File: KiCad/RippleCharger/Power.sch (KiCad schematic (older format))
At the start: 8 parts, among them J1 Screw_Terminal_01x02, U1 L7805

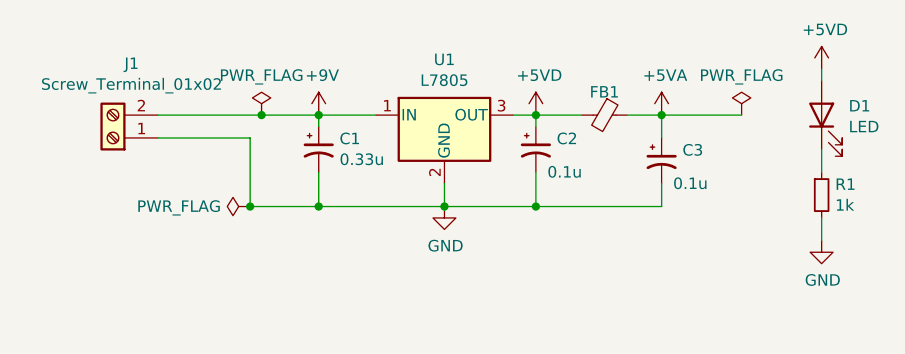
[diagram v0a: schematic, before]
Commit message: Update PCB layout m include relay footprint, board outlook.Modify Main 0049 code and add CV function
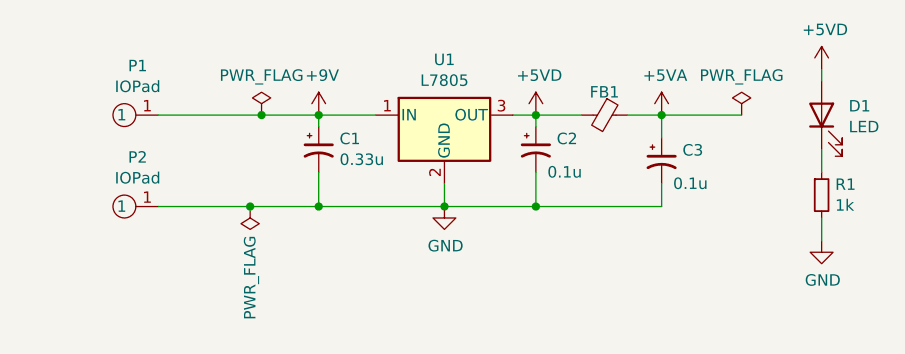
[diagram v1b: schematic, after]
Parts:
- removed J1: Screw_Terminal_01x02, TerminalBlock:TerminalBlock_Altech_AK300-2_P5.00mm, symbol Connector:Screw_Terminal_01x02
- added P1, P2: IOPad, basic:IOPad, symbol basic:IOPad
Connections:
- net +9V: now also P1.1
- net GND: now also P2.1
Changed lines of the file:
@@
 	1    0    0    -1
-$EndComp
-$Comp
-L Connector:Screw_Terminal_01x02 J1
-U 1 1 613EDB5C
-P 3200 3650
-F 0 "J1" H 3118 3325 50  0000 C CNN
-F 1 "Screw_Terminal_01x02" H 3118 3416 50  0000 C CNN
-F 2 "TerminalBlock:TerminalBlock_Altech_AK300-2_P5.00mm" H 3200 3650 50  0001 C CNN
-F 3 "~" H 3200 3650 50  0001 C CNN
-	1    3200 3650
-	-1   0    0    1
 $EndComp
 Wire Wire Line
 	3400 3550 3850 3550
-Wire Wire Line
-	3400 3650 3800 3650
-Wire Wire Line
-	3800 3650 3800 3950
 $Comp
 L power:PWR_FLAG #FLG02
@@
 F 3 "~" H 3800 3950 50  0001 C CNN
 	1    3800 3950
-	0    -1   -1   0
+	-1   0    0    1
 $EndComp
-Connection ~ 3800 3950
 $Comp
 L power:PWR_FLAG #FLG03
@@
 	1    0    0    -1
 $EndComp
+$Comp
+L basic:IOPad P1
+U 1 1 6172F039
+P 3250 3550
+F 0 "P1" H 3192 3335 50  0000 C CNN
+F 1 "IOPad" H 3192 3426 50  0000 C CNN
+F 2 "basic:IOPad" H 3250 3450 50  0001 C CNN
+F 3 "" H 3250 3550 50  0001 C CNN
+	1    3250 3550
+	-1   0    0    1
+$EndComp
+$Comp
+L basic:IOPad P2
+U 1 1 6172FF5A
+P 3250 3950
+F 0 "P2" H 3192 3735 50  0000 C CNN
+F 1 "IOPad" H 3192 3826 50  0000 C CNN
+F 2 "basic:IOPad" H 3250 3850 50  0001 C CNN
+F 3 "" H 3250 3950 50  0001 C CNN
+	1    3250 3950
+	-1   0    0    1
+$EndComp
+Wire Wire Line
+	3400 3950 3800 3950
+Connection ~ 3800 3950
 $EndSCHEMATC
